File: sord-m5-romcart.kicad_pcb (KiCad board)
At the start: 2 copper layers, 99.3 x 62.5 mm, 12 parts, among them SW1 Choose ROM, U2 27C256, U3 74LS00

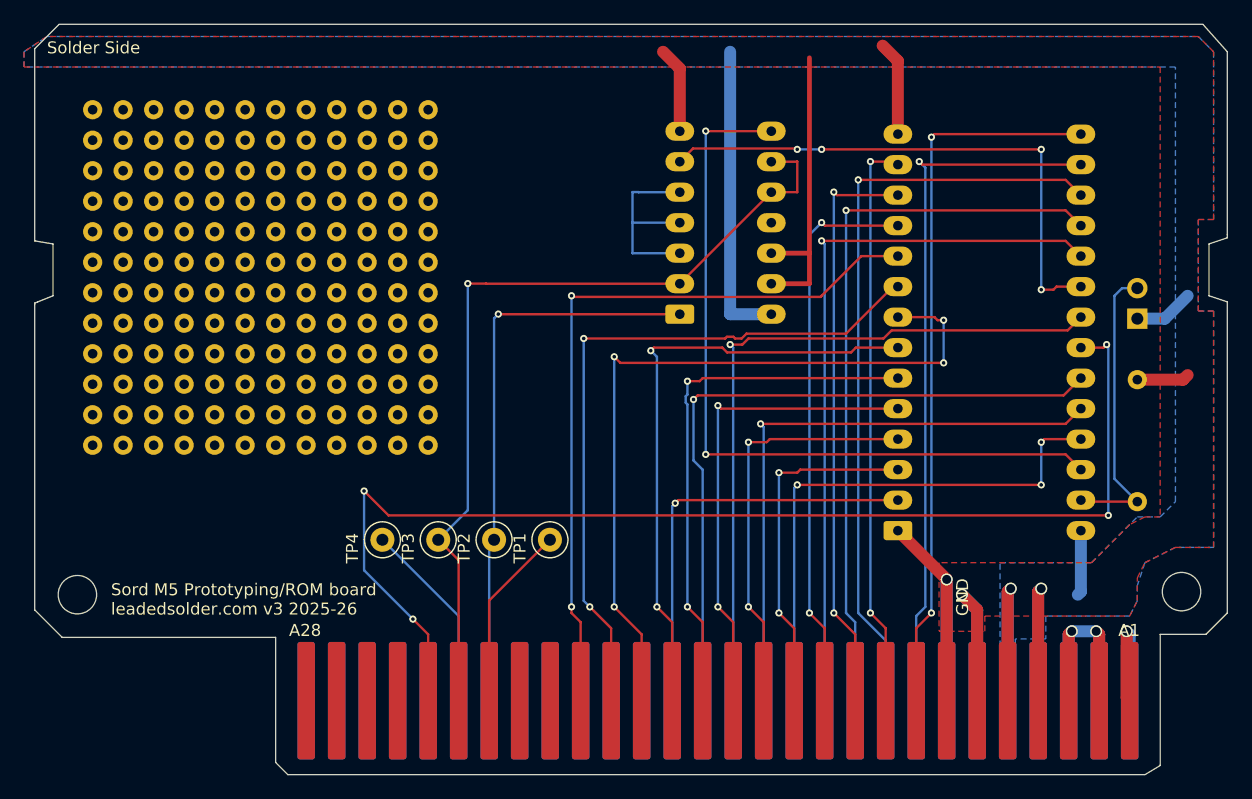
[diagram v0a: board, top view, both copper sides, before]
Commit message: Use AND not NAND
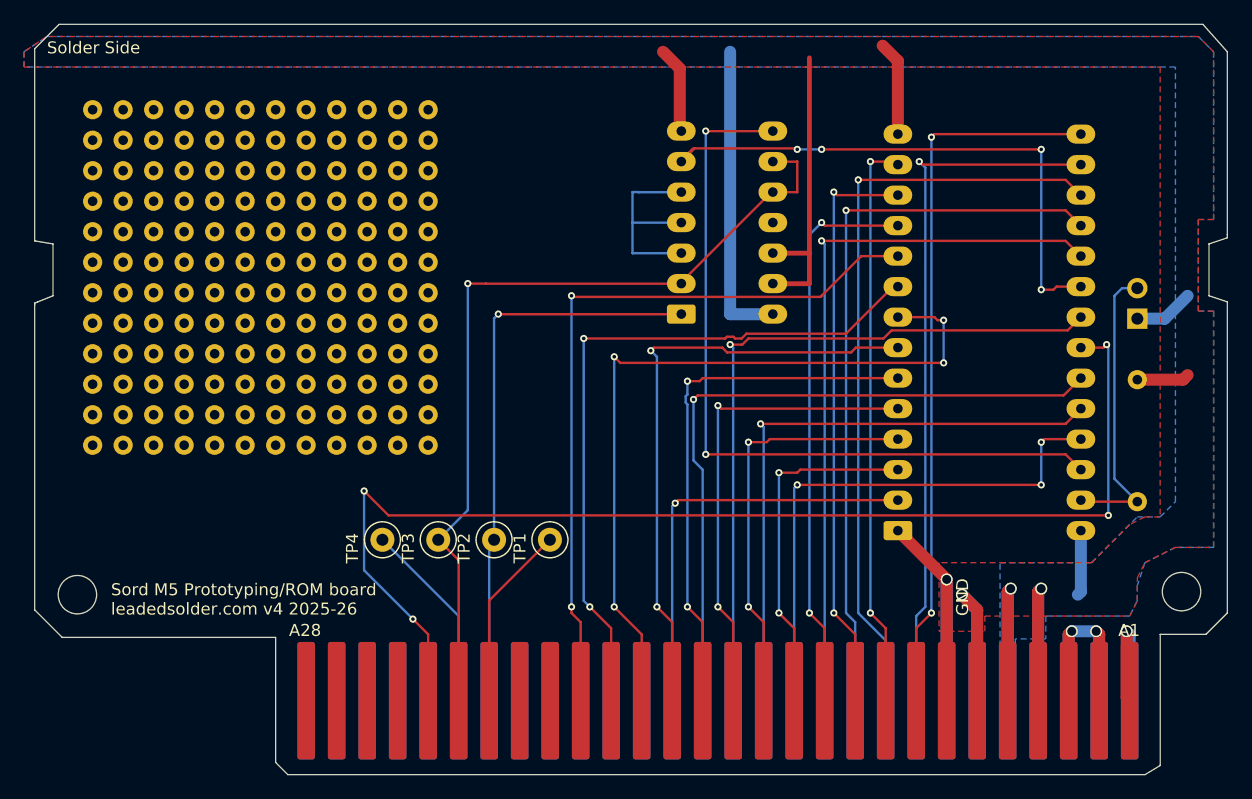
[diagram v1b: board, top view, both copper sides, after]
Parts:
- U3: value 74LS00 -> 74LS08
- moved U3 0.13 mm to (154.4, 115.8)
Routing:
- net /~{ROM_CS}: track 45.7 -> 47.1 mm
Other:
- board text added: "Sord M5 Prototyping/ROM board leadedsolder.com v4 2025-26"
- board text removed: "Sord M5 Prototyping/ROM board leadedsolder.com v3 2025-26"

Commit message: Revert "Use AND not NAND"
This reverts commit 911c91f3a1e7fcb4d358834b32dfa7806c5ac1fb.
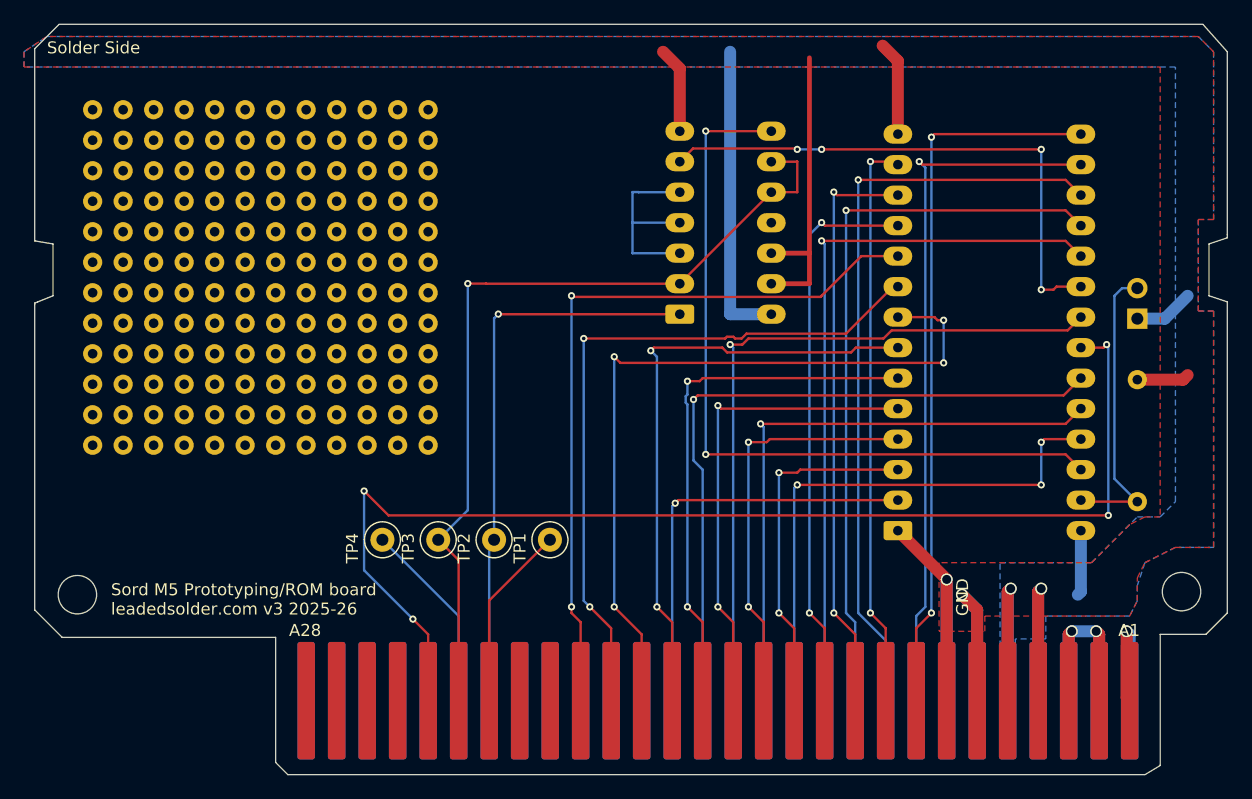
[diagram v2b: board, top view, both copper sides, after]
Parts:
- U3: value 74LS08 -> 74LS00
- moved U3 0.13 mm to (154.3, 115.8)
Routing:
- net /~{ROM_CS}: track 47.1 -> 45.7 mm
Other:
- board text added: "Sord M5 Prototyping/ROM board leadedsolder.com v3 2025-26"
- board text removed: "Sord M5 Prototyping/ROM board leadedsolder.com v4 2025-26"

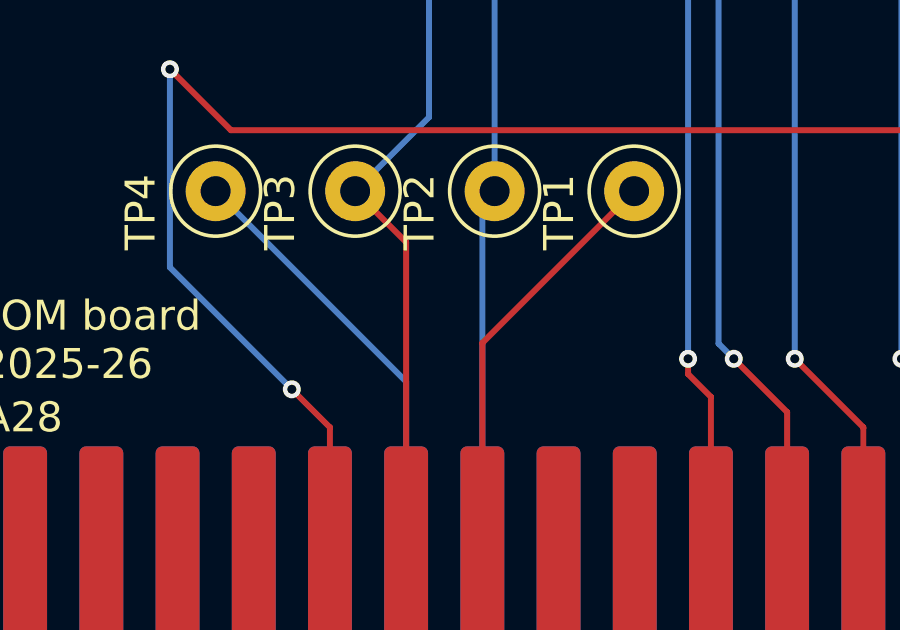
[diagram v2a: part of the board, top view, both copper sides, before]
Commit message: Add tooth labels
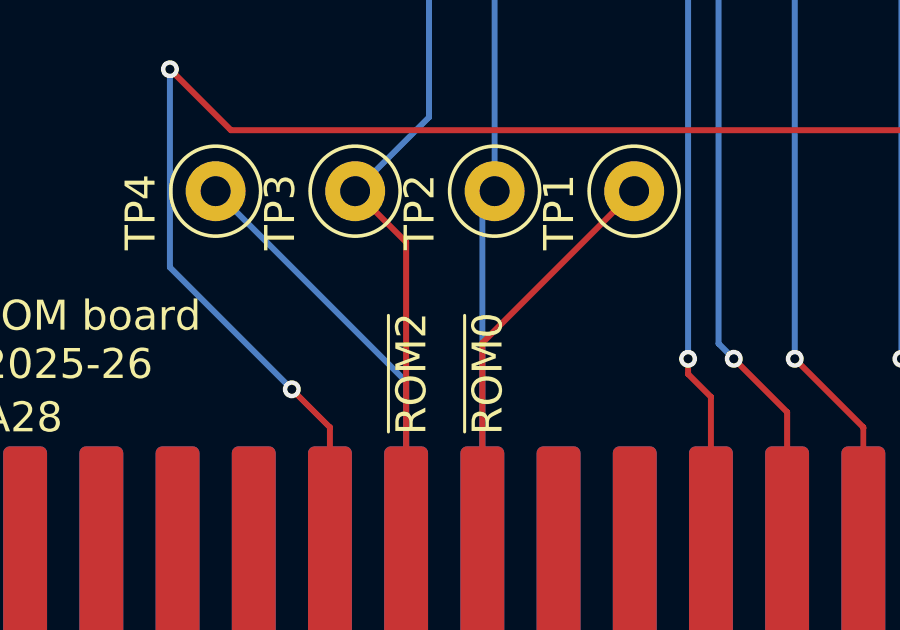
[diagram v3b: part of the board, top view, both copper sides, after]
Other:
- board text added: "~{EXM}"
- board text added: "~{ROM0}"
- board text added: "~{ROM1}"
- board text added: "~{ROM2}"
